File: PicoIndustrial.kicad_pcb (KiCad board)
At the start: 2 copper layers, 140 x 90 mm, 163 parts, among them IC1 LM258D, IC2 LM258D, J1 PICO, J2 WJ15EDGVC-3.81-10P, J3 WJ15EDGVC-3.81-10P, J4 WJ15EDGVC-3.81-10P, J5 WJ15EDGVC-3.81-3P, J6 USB_B_Micro, K1 HF46F_024-HS1T, K2 HF46F_024-HS1T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

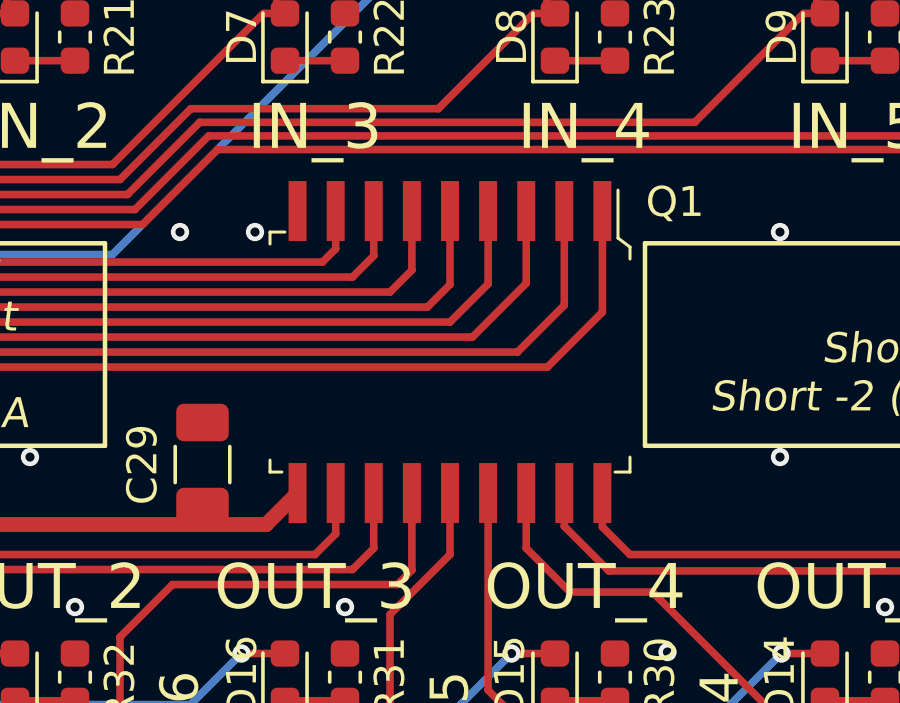
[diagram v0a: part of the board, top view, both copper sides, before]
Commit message: Update 3d modules
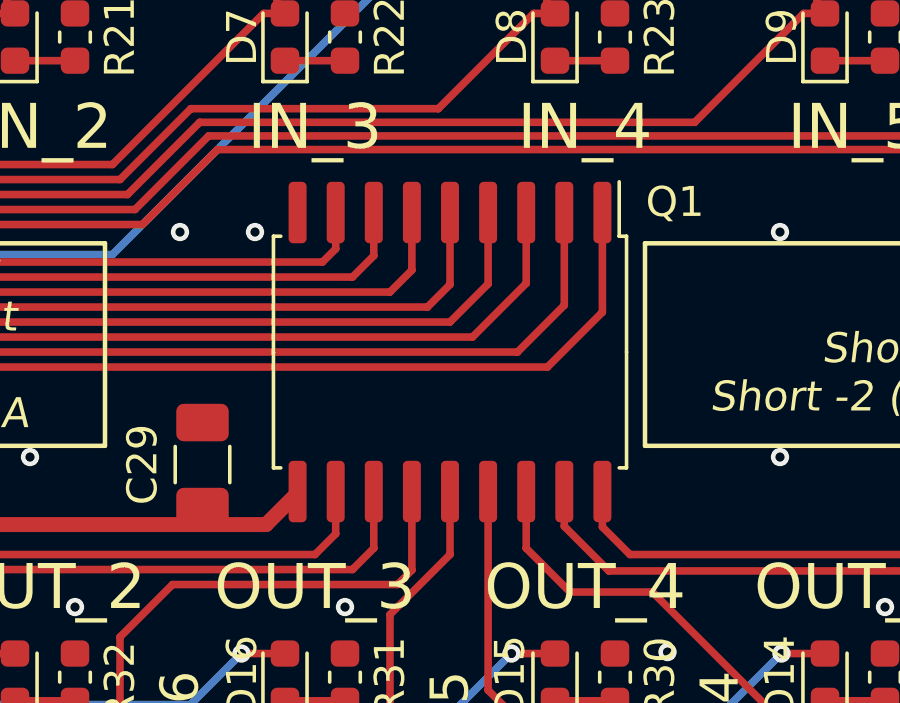
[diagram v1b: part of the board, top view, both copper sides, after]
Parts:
- Q1: footprint digikey-footprints:SOIC-18_W7.5mm -> Package_SO:SOIC-18W_7.5x11.6mm_P1.27mm
- turned Q1 to -90 degrees
